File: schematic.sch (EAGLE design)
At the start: 58 parts, among them U1 ADP3338AKCZ-3.3RL7

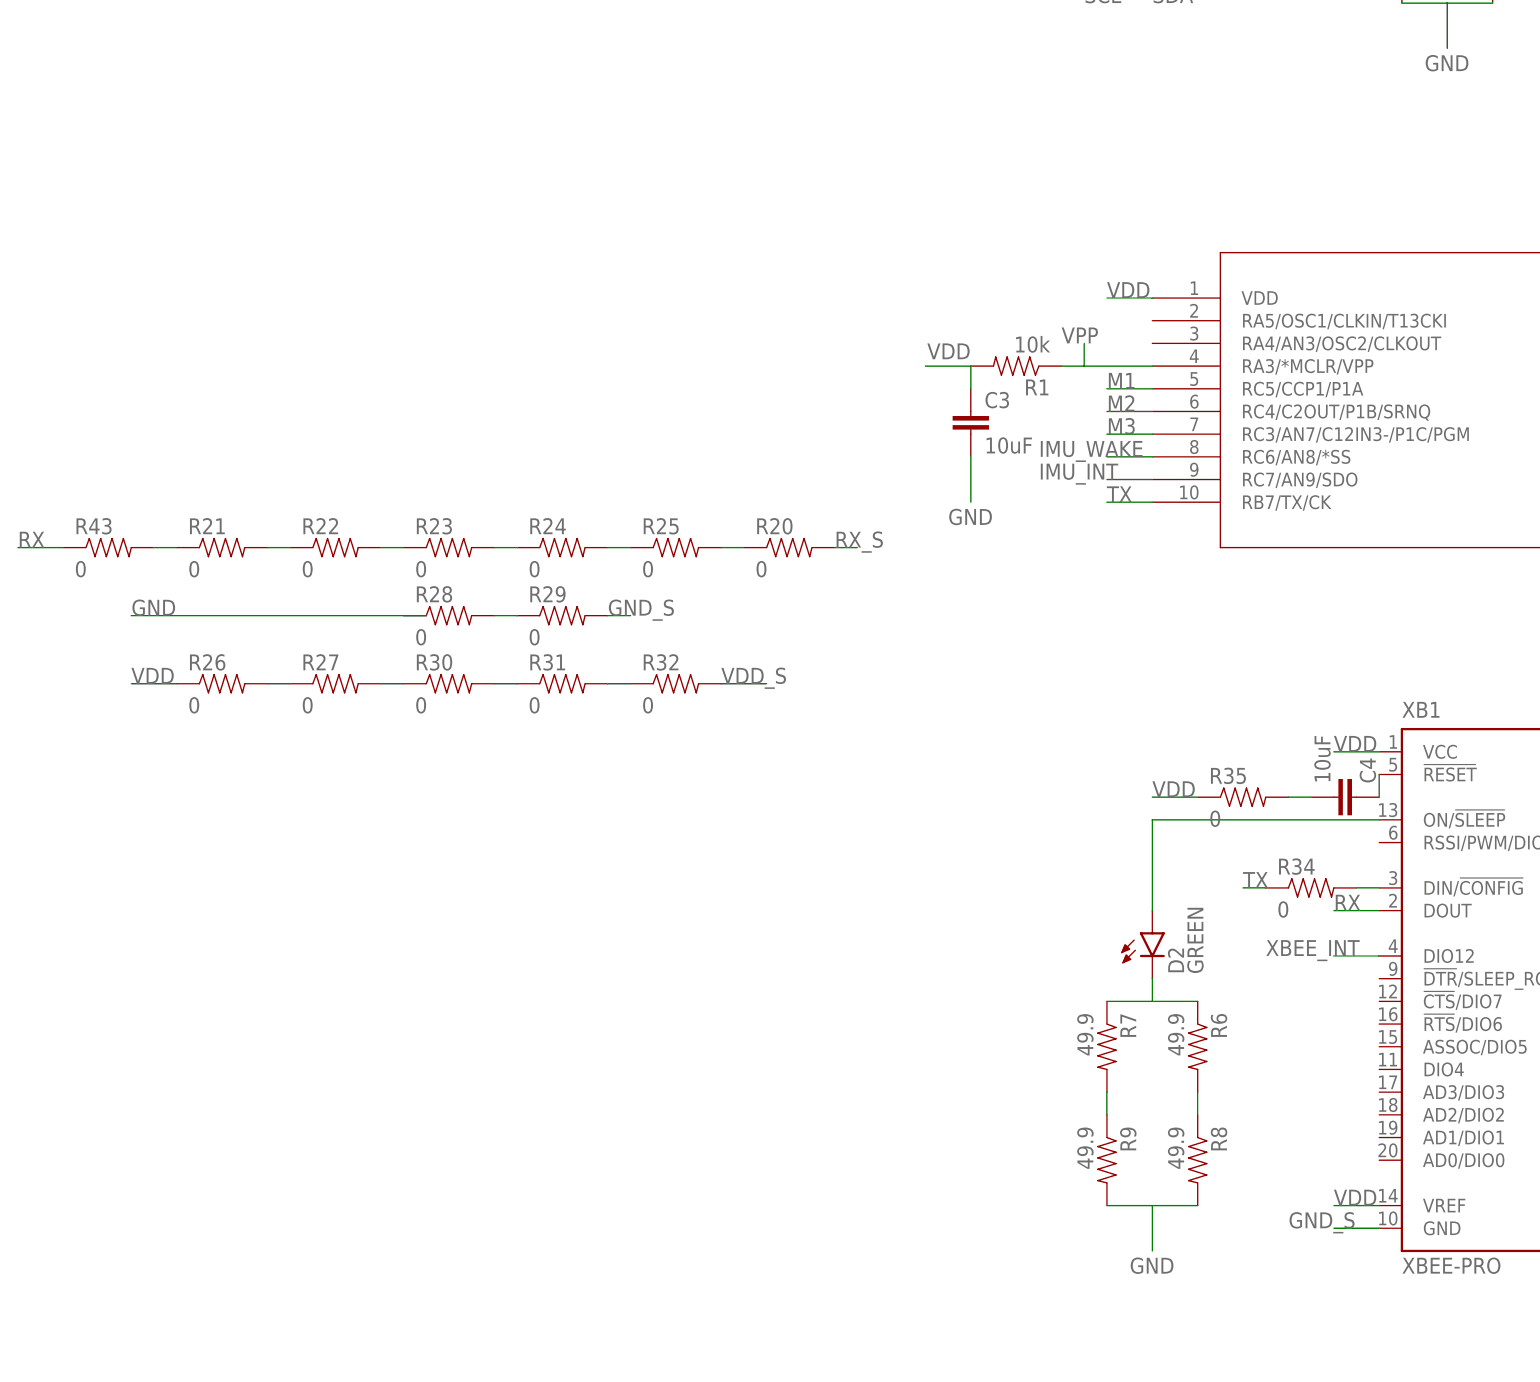
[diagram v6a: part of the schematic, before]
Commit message: Rearanged several components to remove some jumper cables, added led's to unused pins on xbee and controller
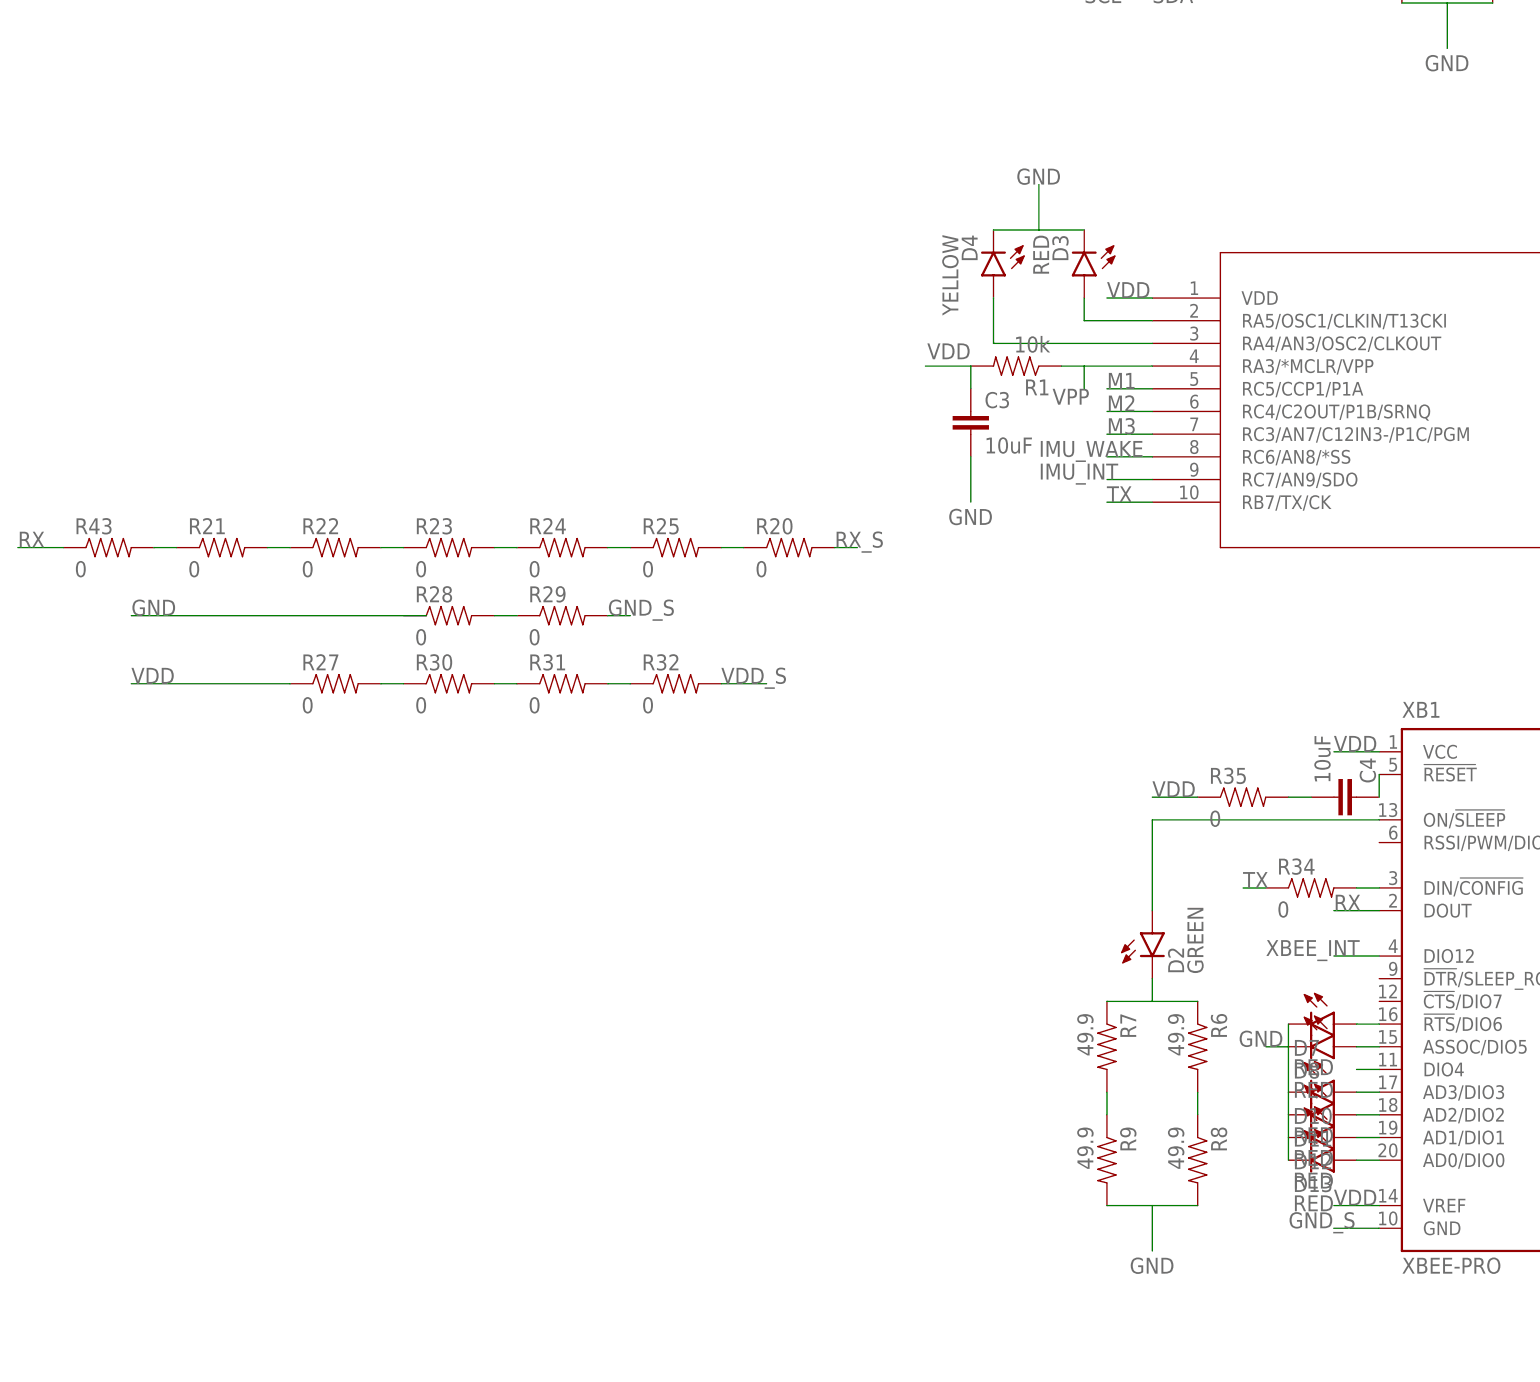
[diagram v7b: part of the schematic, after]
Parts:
- removed R26: 0, SparkFun-Passives:RESISTOR0603-RES
- added D10, D11, D12, D13, D3, D7, D8: RED, SparkFun-LED:LED-RED1206
- added D4: YELLOW, SparkFun-LED:LED-YELLOW1206
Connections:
- removed net N$26: R26.2, R27.1
- new net N$40: D3.A, MAIN_CONTROLLER.RA5/OSC1/CLKIN/T13CKI
- new net N$41: D4.A, MAIN_CONTROLLER.RA4/AN3/OSC2/CLKOUT
- new net N$43: D7.A, XB1.!RTS!/DIO6
- new net N$44: D8.A, XB1.ASSOC/DIO5
- new net N$45: XB1.DIO4
- new net N$46: D10.A, XB1.AD3/DIO3
- new net N$47: D11.A, XB1.AD2/DIO2
- new net N$48: D12.A, XB1.AD1/DIO1
- new net N$49: D13.A, XB1.AD0/DIO0
- net GND: now also D10.C, D11.C, D12.C, D13.C, D3.C, D4.C, D7.C, D8.C
- net VDD: now also R27.1; no longer R26.1
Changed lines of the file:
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@@
 <part name="R28" library="SparkFun-Passives" deviceset="RESISTOR" device="0603-RES" value="0"/>
 <part name="R29" library="SparkFun-Passives" deviceset="RESISTOR" device="0603-RES" value="0"/>
-<part name="R26" library="SparkFun-Passives" deviceset="RESISTOR" device="0603-RES" value="0"/>
 <part name="R27" library="SparkFun-Passives" deviceset="RESISTOR" device="0603-RES" value="0"/>
 <part name="R30" library="SparkFun-Passives" deviceset="RESISTOR" device="0603-RES" value="0"/>
@@
 <part name="R44" library="SparkFun-Passives" deviceset="RESISTOR" device="0603-RES" value="0"/>
 <part name="R45" library="SparkFun-Passives" deviceset="RESISTOR" device="0603-RES" value="0"/>
+<part name="D3" library="SparkFun-LED" deviceset="LED-RED" device="1206" value="RED"/>
+<part name="D4" library="SparkFun-LED" deviceset="LED-YELLOW" device="1206" value="YELLOW"/>
+<part name="D7" library="SparkFun-LED" deviceset="LED-RED" device="1206" value="RED"/>
+<part name="D8" library="SparkFun-LED" deviceset="LED-RED" device="1206" value="RED"/>
+<part name="D10" library="SparkFun-LED" deviceset="LED-RED" device="1206" value="RED"/>
+<part name="D11" library="SparkFun-LED" deviceset="LED-RED" device="1206" value="RED"/>
+<part name="D12" library="SparkFun-LED" deviceset="LED-RED" device="1206" value="RED"/>
+<part name="D13" library="SparkFun-LED" deviceset="LED-RED" device="1206" value="RED"/>
 </parts>
 <sheets>
@@
 <instance part="R28" gate="G$1" x="-78.74" y="-35.56"/>
 <instance part="R29" gate="G$1" x="-66.04" y="-35.56"/>
-<instance part="R26" gate="G$1" x="-104.14" y="-43.18"/>
 <instance part="R27" gate="G$1" x="-91.44" y="-43.18"/>
 <instance part="R30" gate="G$1" x="-78.74" y="-43.18"/>
@@
 <instance part="R44" gate="G$1" x="81.28" y="50.8"/>
 <instance part="R45" gate="G$1" x="175.26" y="-22.86"/>
+<instance part="D3" gate="G$1" x="-7.62" y="2.54" rot="R180"/>
+<instance part="D4" gate="G$1" x="-17.78" y="2.54" rot="R180"/>
+<instance part="D7" gate="G$1" x="20.32" y="-81.28" rot="R270"/>
+<instance part="D8" gate="G$1" x="20.32" y="-83.82" rot="R270"/>
+<instance part="D10" gate="G$1" x="20.32" y="-88.9" rot="R270"/>
+<instance part="D11" gate="G$1" x="20.32" y="-91.44" rot="R270"/>
+<instance part="D12" gate="G$1" x="20.32" y="-93.98" rot="R270"/>
+<instance part="D13" gate="G$1" x="20.32" y="-96.52" rot="R270"/>
 </instances>
 <busses>
@@
 <wire x1="-10.16" y1="-7.62" x2="-7.62" y2="-7.62" width="0.1524" layer="91"/>
 <wire x1="-7.62" y1="-7.62" x2="0" y2="-7.62" width="0.1524" layer="91"/>
-<wire x1="-7.62" y1="-7.62" x2="-7.62" y2="-5.08" width="0.1524" layer="91"/>
-<label x="-10.16" y="-5.08" size="1.778" layer="95"/>
+<wire x1="-7.62" y1="-7.62" x2="-7.62" y2="-10.16" width="0.1524" layer="91"/>
+<label x="-11.176" y="-11.938" size="1.778" layer="95"/>
 </segment>
 </net>
@@
 </segment>
 <segment>
-<pinref part="R26" gate="G$1" pin="1"/>
-<wire x1="-109.22" y1="-43.18" x2="-114.3" y2="-43.18" width="0.1524" layer="91"/>
 <label x="-114.3" y="-43.18" size="1.778" layer="95"/>
+<pinref part="R27" gate="G$1" pin="1"/>
+<wire x1="-114.3" y1="-43.18" x2="-96.52" y2="-43.18" width="0.1524" layer="91"/>
 </segment>
 <segment>
@@
 <label x="187.96" y="-58.42" size="1.778" layer="95"/>
 </segment>
+<segment>
+<pinref part="D4" gate="G$1" pin="C"/>
+<pinref part="D3" gate="G$1" pin="C"/>
+<wire x1="-17.78" y1="7.62" x2="-12.7" y2="7.62" width="0.1524" layer="91"/>
+<wire x1="-12.7" y1="7.62" x2="-7.62" y2="7.62" width="0.1524" layer="91"/>
+<wire x1="-12.7" y1="7.62" x2="-12.7" y2="12.7" width="0.1524" layer="91"/>
+<label x="-15.24" y="12.7" size="1.778" layer="95"/>
+</segment>
+<segment>
+<pinref part="D7" gate="G$1" pin="C"/>
+<pinref part="D8" gate="G$1" pin="C"/>
+<wire x1="15.24" y1="-81.28" x2="15.24" y2="-83.82" width="0.1524" layer="91"/>
+<pinref part="D10" gate="G$1" pin="C"/>
+<wire x1="15.24" y1="-83.82" x2="15.24" y2="-88.9" width="0.1524" layer="91"/>
+<pinref part="D11" gate="G$1" pin="C"/>
+<wire x1="15.24" y1="-88.9" x2="15.24" y2="-91.44" width="0.1524" layer="91"/>
+<pinref part="D12" gate="G$1" pin="C"/>
+<wire x1="15.24" y1="-91.44" x2="15.24" y2="-93.98" width="0.1524" layer="91"/>
+<pinref part="D13" gate="G$1" pin="C"/>
+<wire x1="15.24" y1="-93.98" x2="15.24" y2="-96.52" width="0.1524" layer="91"/>
+<wire x1="15.24" y1="-83.82" x2="12.7" y2="-83.82" width="0.1524" layer="91"/>
+<label x="9.652" y="-83.82" size="1.778" layer="95"/>
+</segment>
 </net>
 <net name="M1" class="0">
@@
 <pinref part="R29" gate="G$1" pin="1"/>
 <wire x1="-73.66" y1="-35.56" x2="-71.12" y2="-35.56" width="0.1524" layer="91"/>
-</segment>
-</net>
-<net name="N$26" class="0">
-<segment>
-<pinref part="R26" gate="G$1" pin="2"/>
-<pinref part="R27" gate="G$1" pin="1"/>
-<wire x1="-99.06" y1="-43.18" x2="-96.52" y2="-43.18" width="0.1524" layer="91"/>
 </segment>
 </net>
@@
 </segment>
 </net>
+<net name="N$40" class="0">
+<segment>
+<pinref part="MAIN_CONTROLLER" gate="A" pin="RA5/OSC1/CLKIN/T13CKI"/>
+<pinref part="D3" gate="G$1" pin="A"/>
+<wire x1="0" y1="-2.54" x2="-7.62" y2="-2.54" width="0.1524" layer="91"/>
+<wire x1="-7.62" y1="-2.54" x2="-7.62" y2="0" width="0.1524" layer="91"/>
+</segment>
+</net>
+<net name="N$41" class="0">
+<segment>
+<pinref part="MAIN_CONTROLLER" gate="A" pin="RA4/AN3/OSC2/CLKOUT"/>
+<pinref part="D4" gate="G$1" pin="A"/>
+<wire x1="0" y1="-5.08" x2="-17.78" y2="-5.08" width="0.1524" layer="91"/>
+<wire x1="-17.78" y1="-5.08" x2="-17.78" y2="0" width="0.1524" layer="91"/>
+</segment>
+</net>
+<net name="N$43" class="0">
+<segment>
+<pinref part="XB1" gate="G$1" pin="!RTS!/DIO6"/>
+<pinref part="D7" gate="G$1" pin="A"/>
+<wire x1="25.4" y1="-81.28" x2="22.86" y2="-81.28" width="0.1524" layer="91"/>
+</segment>
+</net>
+<net name="N$44" class="0">
+<segment>
+<pinref part="XB1" gate="G$1" pin="ASSOC/DIO5"/>
+<pinref part="D8" gate="G$1" pin="A"/>
+<wire x1="25.4" y1="-83.82" x2="22.86" y2="-83.82" width="0.1524" layer="91"/>
+</segment>
+</net>
+<net name="N$45" class="0">
+<segment>
+<pinref part="XB1" gate="G$1" pin="DIO4"/>
+<wire x1="25.4" y1="-86.36" x2="22.86" y2="-86.36" width="0.1524" layer="91"/>
+</segment>
+</net>
+<net name="N$46" class="0">
+<segment>
+<pinref part="XB1" gate="G$1" pin="AD3/DIO3"/>
+<pinref part="D10" gate="G$1" pin="A"/>
+<wire x1="25.4" y1="-88.9" x2="22.86" y2="-88.9" width="0.1524" layer="91"/>
+</segment>
+</net>
+<net name="N$47" class="0">
+<segment>
+<pinref part="XB1" gate="G$1" pin="AD2/DIO2"/>
+<pinref part="D11" gate="G$1" pin="A"/>
+<wire x1="25.4" y1="-91.44" x2="22.86" y2="-91.44" width="0.1524" layer="91"/>
+</segment>
+</net>
+<net name="N$48" class="0">
+<segment>
+<pinref part="XB1" gate="G$1" pin="AD1/DIO1"/>
+<pinref part="D12" gate="G$1" pin="A"/>
+<wire x1="25.4" y1="-93.98" x2="22.86" y2="-93.98" width="0.1524" layer="91"/>
+</segment>
+</net>
+<net name="N$49" class="0">
+<segment>
+<pinref part="XB1" gate="G$1" pin="AD0/DIO0"/>
+<pinref part="D13" gate="G$1" pin="A"/>
+<wire x1="25.4" y1="-96.52" x2="22.86" y2="-96.52" width="0.1524" layer="91"/>
+</segment>
+</net>
